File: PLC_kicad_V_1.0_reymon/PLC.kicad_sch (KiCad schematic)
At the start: 0 parts

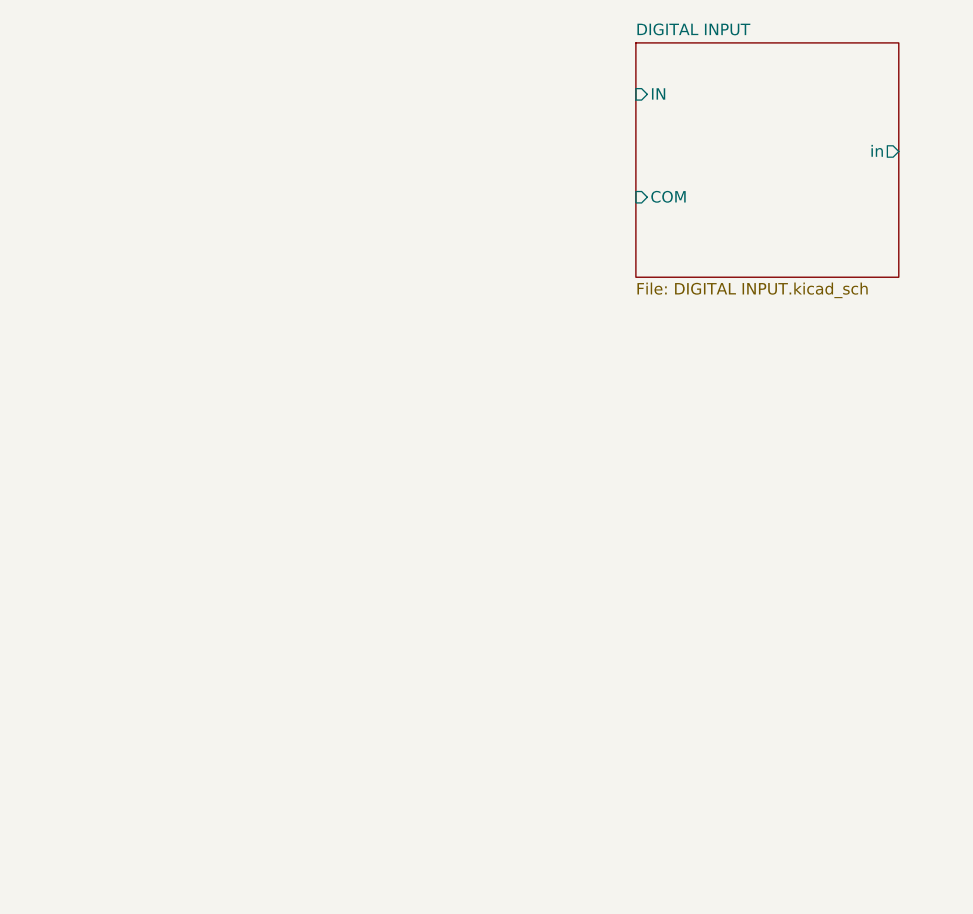
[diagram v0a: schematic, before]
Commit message: fotos de circuitos investigado, diagramas de bloque de estos circuitos<aun en proceso>,se anadio zip y lck al gitignore, y subir pcb_mezzanine con ajuste de tamano y plano de tierra<aun en proceso de configuracion de stack up y demas>
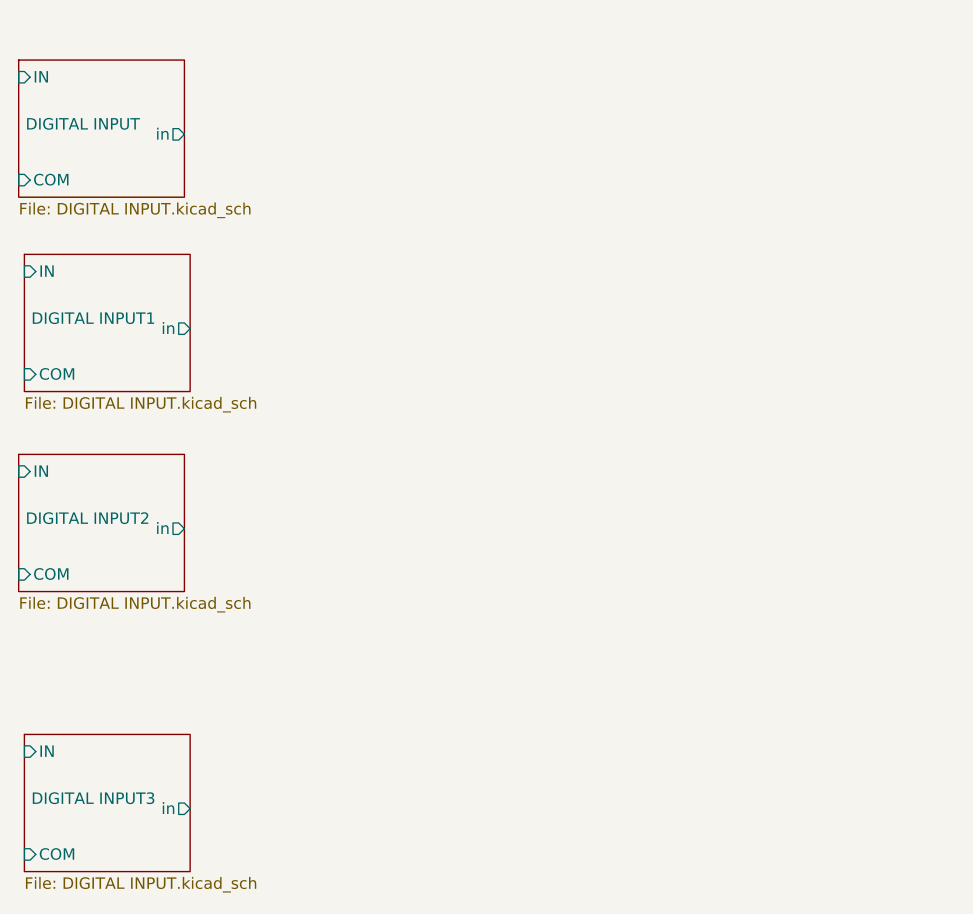
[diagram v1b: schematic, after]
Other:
- added sheet DIGITAL INPUT1 (DIGITAL INPUT.kicad_sch)
- added sheet DIGITAL INPUT2 (DIGITAL INPUT.kicad_sch)
- added sheet DIGITAL INPUT3 (DIGITAL INPUT.kicad_sch)
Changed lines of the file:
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@@
 	(paper "A4")
 	(sheet
-		(at 97.79 42.545)
-		(size 29.21 26.035)
-		(exclude_from_sim no)
-		(in_bom yes)
-		(on_board yes)
-		(dnp no)
-		(fields_autoplaced yes)
+		(at 29.845 119.38)
+		(size 18.415 15.24)
+		(exclude_from_sim no)
+		(in_bom yes)
+		(on_board yes)
+		(dnp no)
+		(stroke
+			(width 0.1524)
+			(type solid)
+		)
+		(fill
+			(color 255 226 54 1.0000)
+		)
+		(property "Sheetname" "DIGITAL INPUT3"
+			(at 30.607 127.254 0)
+			(effects
+				(font
+					(size 1.27 1.27)
+				)
+				(justify left bottom)
+			)
+		)
+		(property "Sheetfile" "DIGITAL INPUT.kicad_sch"
+			(at 29.845 135.2046 0)
+			(effects
+				(font
+					(size 1.27 1.27)
+				)
+				(justify left top)
+			)
+		)
+		(pin "IN" input
+			(at 29.845 121.285 180)
+			(effects
+				(font
+					(size 1.27 1.27)
+				)
+				(justify left)
+			)
+		)
+		(pin "COM" input
+			(at 29.845 132.715 180)
+			(effects
+				(font
+					(size 1.27 1.27)
+				)
+				(justify left)
+			)
+		)
+		(pin "in" output
+			(at 48.26 127.635 0)
+			(effects
+				(font
+					(size 1.27 1.27)
+				)
+				(justify right)
+			)
+		)
+		(instances
+			(project "PLC"
+				(path "/3e78205a-c5f6-4422-8d57-aad5ffe102ef"
+					(page "5")
+				)
+			)
+		)
+	)
+	(sheet
+		(at 29.21 44.45)
+		(size 18.415 15.24)
+		(exclude_from_sim no)
+		(in_bom yes)
+		(on_board yes)
+		(dnp no)
 		(stroke
 			(width 0.1524)
@@
 		)
 		(property "Sheetname" "DIGITAL INPUT"
-			(at 97.79 41.8334 0)
-			(effects
-				(font
-					(size 1.27 1.27)
-				)
-				(justify left bottom)
-			)
-		)
-		(property "Sheetfile" "DIGITAL INPUT.kicad_sch"
-			(at 97.79 69.1646 0)
-			(effects
-				(font
-					(size 1.27 1.27)
-				)
-				(justify left top)
-			)
-		)
-		(pin "IN" input
-			(at 97.79 48.26 180)
-			(effects
-				(font
-					(size 1.27 1.27)
-				)
-				(justify left)
-			)
-		)
-		(pin "COM" input
-			(at 97.79 59.69 180)
-			(effects
-				(font
-					(size 1.27 1.27)
-				)
-				(justify left)
-			)
-		)
-		(pin "in" output
-			(at 127 54.61 0)
+			(at 29.972 52.324 0)
+			(effects
+				(font
+					(size 1.27 1.27)
+				)
+				(justify left bottom)
+			)
+		)
+		(property "Sheetfile" "DIGITAL INPUT.kicad_sch"
+			(at 29.21 60.2746 0)
+			(effects
+				(font
+					(size 1.27 1.27)
+				)
+				(justify left top)
+			)
+		)
+		(pin "IN" input
+			(at 29.21 46.355 180)
+			(effects
+				(font
+					(size 1.27 1.27)
+				)
+				(justify left)
+			)
+		)
+		(pin "COM" input
+			(at 29.21 57.785 180)
+			(effects
+				(font
+					(size 1.27 1.27)
+				)
+				(justify left)
+			)
+		)
+		(pin "in" output
+			(at 47.625 52.705 0)
 			(effects
 				(font
@@
 				)
 			)
+		)
+	)
+	(sheet
+		(at 29.845 66.04)
+		(size 18.415 15.24)
+		(exclude_from_sim no)
+		(in_bom yes)
+		(on_board yes)
+		(dnp no)
+		(stroke
+			(width 0.1524)
+			(type solid)
+		)
+		(fill
+			(color 255 226 54 1.0000)
+		)
+		(property "Sheetname" "DIGITAL INPUT1"
+			(at 30.607 73.914 0)
+			(effects
+				(font
+					(size 1.27 1.27)
+				)
+				(justify left bottom)
+			)
+		)
+		(property "Sheetfile" "DIGITAL INPUT.kicad_sch"
+			(at 29.845 81.8646 0)
+			(effects
+				(font
+					(size 1.27 1.27)
+				)
+				(justify left top)
+			)
+		)
+		(pin "IN" input
+			(at 29.845 67.945 180)
+			(effects
+				(font
+					(size 1.27 1.27)
+				)
+				(justify left)
+			)
+		)
+		(pin "COM" input
+			(at 29.845 79.375 180)
+			(effects
+				(font
+					(size 1.27 1.27)
+				)
+				(justify left)
+			)
+		)
+		(pin "in" output
+			(at 48.26 74.295 0)
+			(effects
+				(font
+					(size 1.27 1.27)
+				)
+				(justify right)
+			)
+		)
+		(instances
+			(project "PLC"
+				(path "/3e78205a-c5f6-4422-8d57-aad5ffe102ef"
+					(page "3")
+				)
+			)
+		)
+	)
+	(sheet
+		(at 29.21 88.265)
+		(size 18.415 15.24)
+		(exclude_from_sim no)
+		(in_bom yes)
+		(on_board yes)
+		(dnp no)
+		(stroke
+			(width 0.1524)
+			(type solid)
+		)
+		(fill
+			(color 255 226 54 1.0000)
+		)
+		(property "Sheetname" "DIGITAL INPUT2"
+			(at 29.972 96.139 0)
+			(effects
+				(font
+					(size 1.27 1.27)
+				)
+				(justify left bottom)
+			)
+		)
+		(property "Sheetfile" "DIGITAL INPUT.kicad_sch"
+			(at 29.21 104.0896 0)
+			(effects
+				(font
+					(size 1.27 1.27)
+				)
+				(justify left top)
+			)
+		)
+		(pin "IN" input
+			(at 29.21 90.17 180)
+			(effects
+				(font
+					(size 1.27 1.27)
+				)
+				(justify left)
+			)
+		)
+		(pin "COM" input
+			(at 29.21 101.6 180)
+			(effects
+				(font
+					(size 1.27 1.27)
+				)
+				(justify left)
+			)
+		)
+		(pin "in" output
+			(at 47.625 96.52 0)
+			(effects
+				(font
+					(size 1.27 1.27)
+				)
+				(justify right)
+			)
+		)
+		(instances
+			(project "PLC"
+				(path "/3e78205a-c5f6-4422-8d57-aad5ffe102ef"
+					(page "4")
+				)
+			)
